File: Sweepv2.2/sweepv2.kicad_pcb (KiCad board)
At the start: 2 copper layers, 216.9 x 86.9 mm, 51 parts, among them J1 AudioJack4dpb, J2 AudioJack4dpb, SW10 SW_Push, SW11 SW_Push, SW11_r1 SW_Push, SW12 SW_Push, SW12_r1 SW_Push, SW13_r1 SW_Push, SW14 SW_Push, SW15 SW_Push, SW15_r1 SW_Push, SW16 SW_Push, SW16_r1 SW_Push, SW17 SW_Push, SW17_r1 SW_Push, SW18 SW_Push, SW18_r1 SW_Push, SW2 SW_Push, SW20 SW_Push, SW20_r1 SW_Push, SW21 SW_Push, SW21_r1 SW_Push, SW2_r1 SW_Push, SW3 SW_Push, SW3_r1 SW_Push, SW4 SW_Push, SW4_r1 SW_Push, SW5 SW_Push, SW5_r1 SW_Push, SW6 SW_Push, SW6_r1 SW_Push, SW7_r1 SW_Push, SW8 SW_Push, SW8_r1 SW_Push, SW9 SW_Push, SW9_r1 SW_Push, U1 ProMicro-kbd, U2 ProMicro-kbd

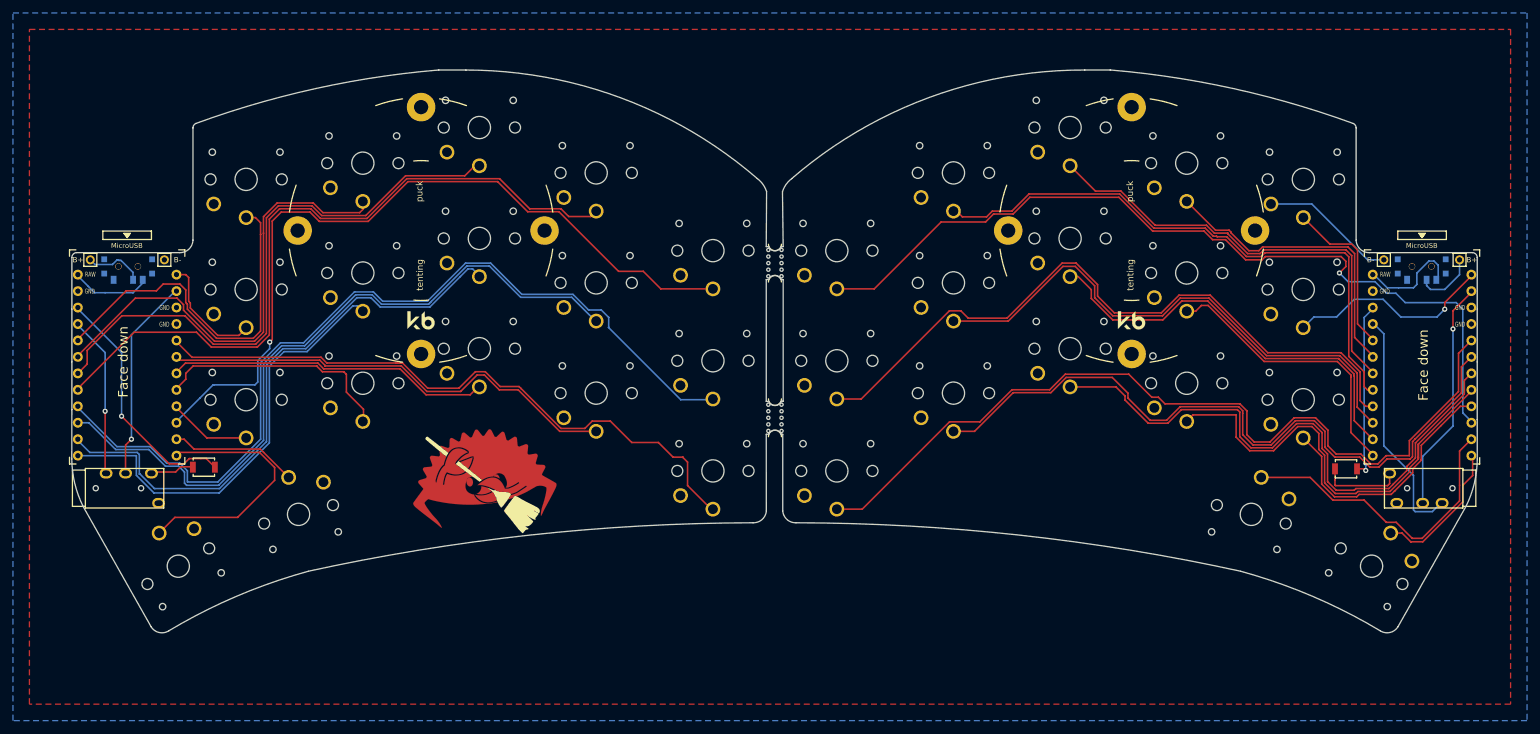
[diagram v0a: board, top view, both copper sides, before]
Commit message: feat: Tweak sweepv2.2 PCB shape and design
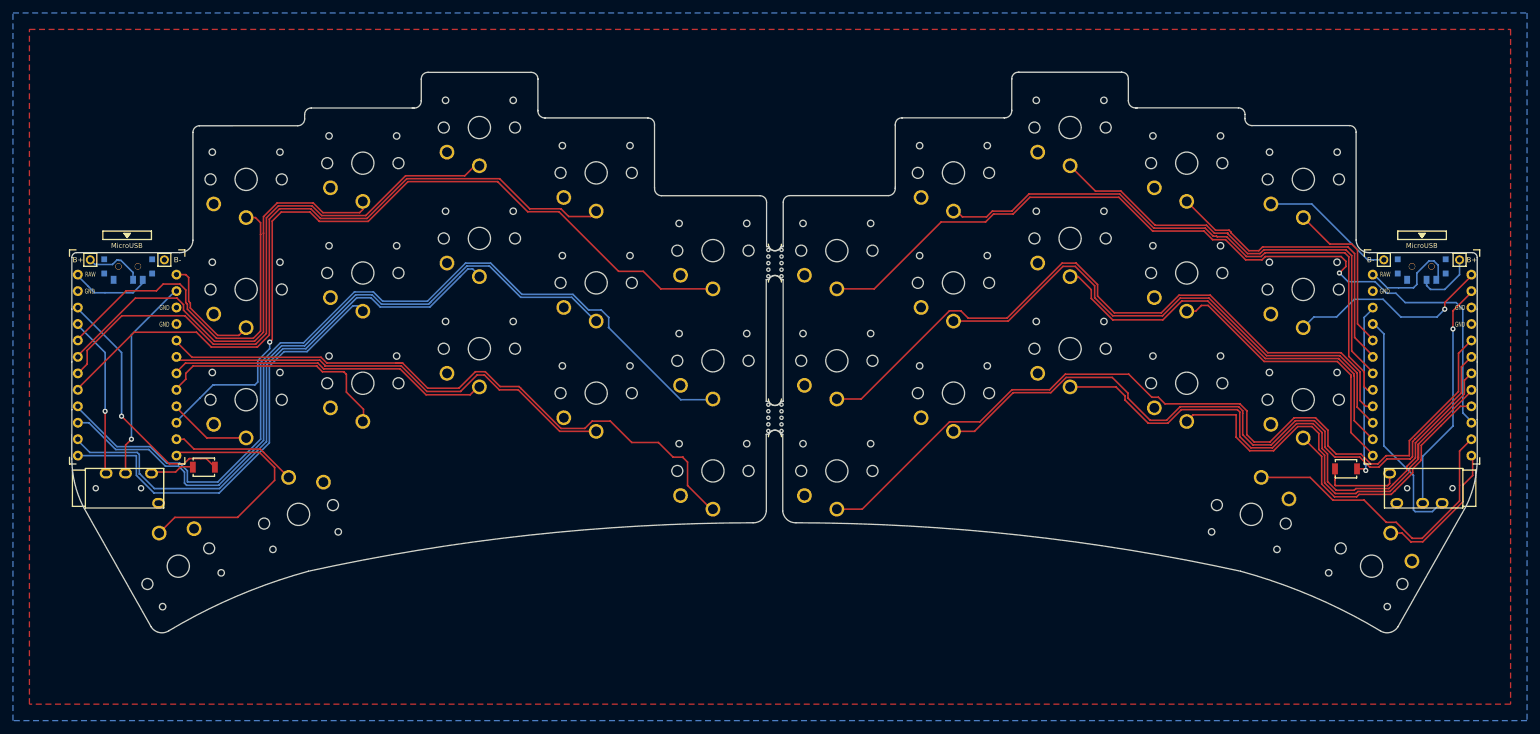
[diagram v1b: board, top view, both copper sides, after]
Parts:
- removed the G*** at (84.1, 85.3)
- removed REF** (x2): Tenting Puck, kbd:Tenting_Puck2
- added G***: LOGO, Ferris:ferris_mask, F.Cu at (83.5, 84.7)
- added G***: LOGO, Ferris:corro_mask, F.Cu at (177.1, 83.1)
- added G***: LOGO, Ferris:ferris_silkscreen_large, B.Cu at (82.0, 57.5)
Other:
- board size 216.9 x 86.9 mm -> 216.9 x 86.5 mm
- board text added: "ferris-sweep rev. 0.1"
- board text removed: "Face down"
- board text removed: "Sweep is based on the Ferris."
- board text removed: "Sweep v 2.2"
